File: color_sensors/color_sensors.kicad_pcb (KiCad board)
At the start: 2 copper layers, 42 x 22 mm, 10 parts, among them J1 22-05-7048-04, Q1 TEPT4400, Q2 TEPT4400, U1 LM358

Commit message: Submission candidate 1
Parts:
- added C1: 100n, IDP_library_C025-024X044, F.Cu at (156.5, 92.0)
- J1: footprint IDP:IDP_library_7395-04 -> IDP_library_7395-04
- R1, R2: value 27k -> 7.5k
- R3, R4: value 6.8k -> 4.7k
- U1: value LM358 -> LM393
- moved R1 64.7 mm to (159.0, 94.5)
- moved J1 64.3 mm to (140.0, 88.0)
- moved Q1 64.3 mm to (156.5, 86.5)
- moved Q2 64.3 mm to (162.5, 86.5)
- moved R2 64.3 mm to (162.5, 94.5)
- moved R3 64.3 mm to (144.5, 97.0)
- moved R4 64.3 mm to (152.0, 97.0)
- moved U1 64.3 mm to (148.0, 90.0)
- moved VR1 64.3 mm to (149.0, 81.5)
- moved VR2 64.3 mm to (159.5, 81.5)
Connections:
- VR1 pad 2: Net-(VR1-Pad2) -> GND
- VR1 pad 3: GND -> Net-(VR1-Pad3)
- VR2 pad 2: Net-(VR2-Pad2) -> GND
- VR2 pad 3: GND -> Net-(VR2-Pad3)
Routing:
- net +5V: track 34.7 -> 49.4 mm
- net GND: track 45.7 -> 50.8 mm

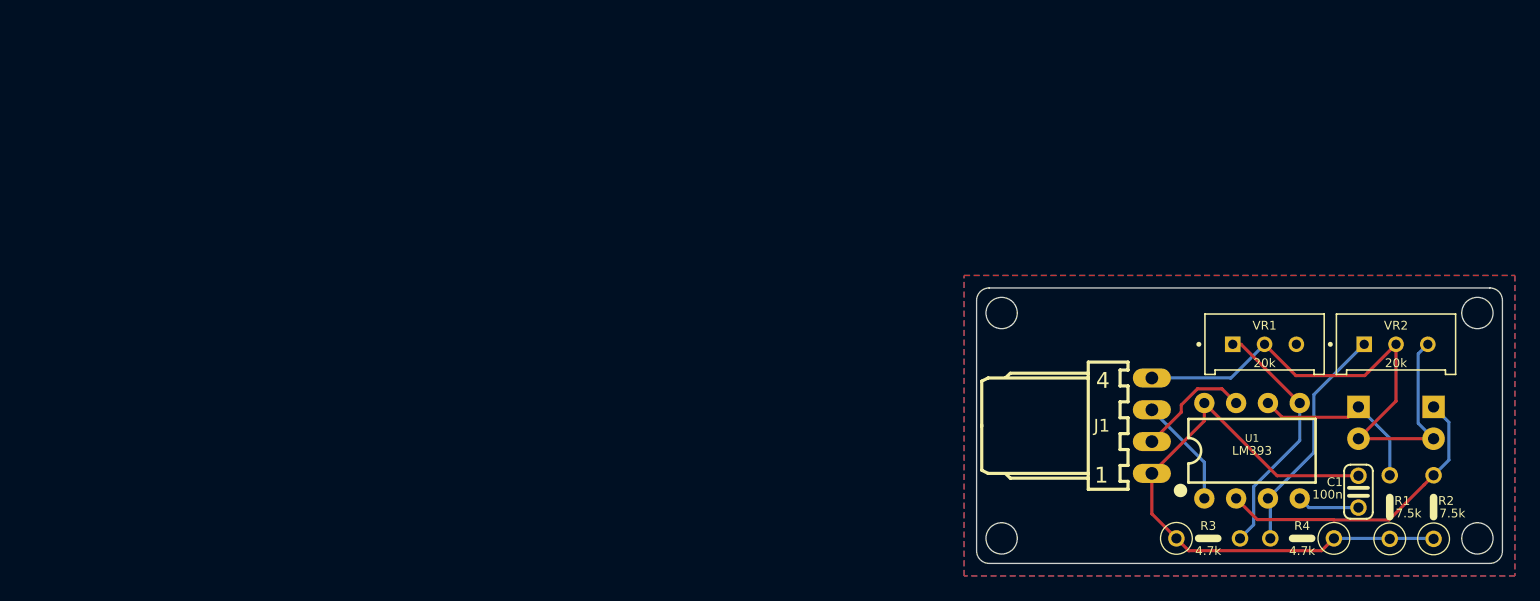
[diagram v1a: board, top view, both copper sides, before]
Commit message: Add PDF versions of schematics
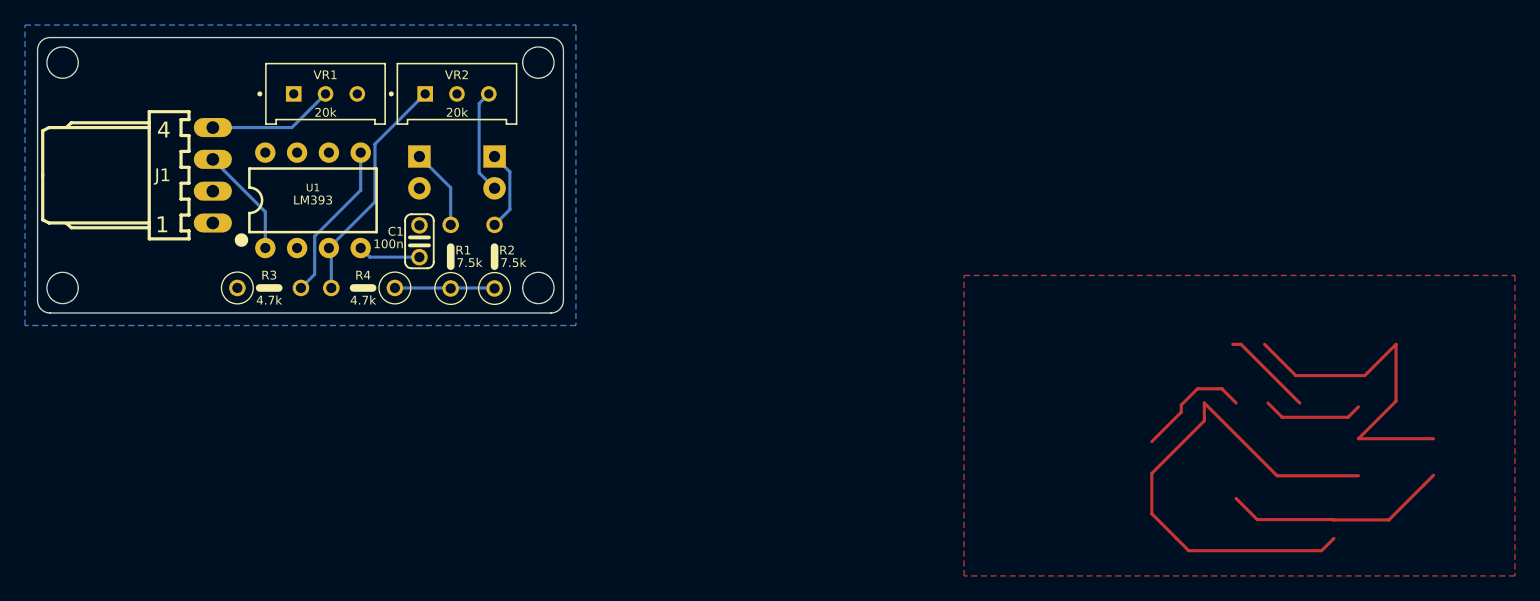
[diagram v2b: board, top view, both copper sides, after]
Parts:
- moved C1 77.6 mm to (81.5, 72.0)
- moved J1 77.6 mm to (65.0, 68.0)
- moved Q1 77.6 mm to (81.5, 66.5)
- moved Q2 77.6 mm to (87.5, 66.5)
- moved R1 77.6 mm to (84.0, 74.5)
- moved R2 77.6 mm to (87.5, 74.5)
- moved R3 77.6 mm to (69.5, 77.0)
- moved R4 77.6 mm to (77.0, 77.0)
- moved U1 77.6 mm to (73.0, 70.0)
- moved VR1 77.6 mm to (74.0, 61.5)
- moved VR2 77.6 mm to (84.5, 61.5)
